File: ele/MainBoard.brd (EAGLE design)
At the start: 149.3 x 100 mm, 114 parts, among them IC1 MCP23017SP, IC2 74HC595D, IC3 74HC595D, X1 POWER_IN, X2 POWER_OUT

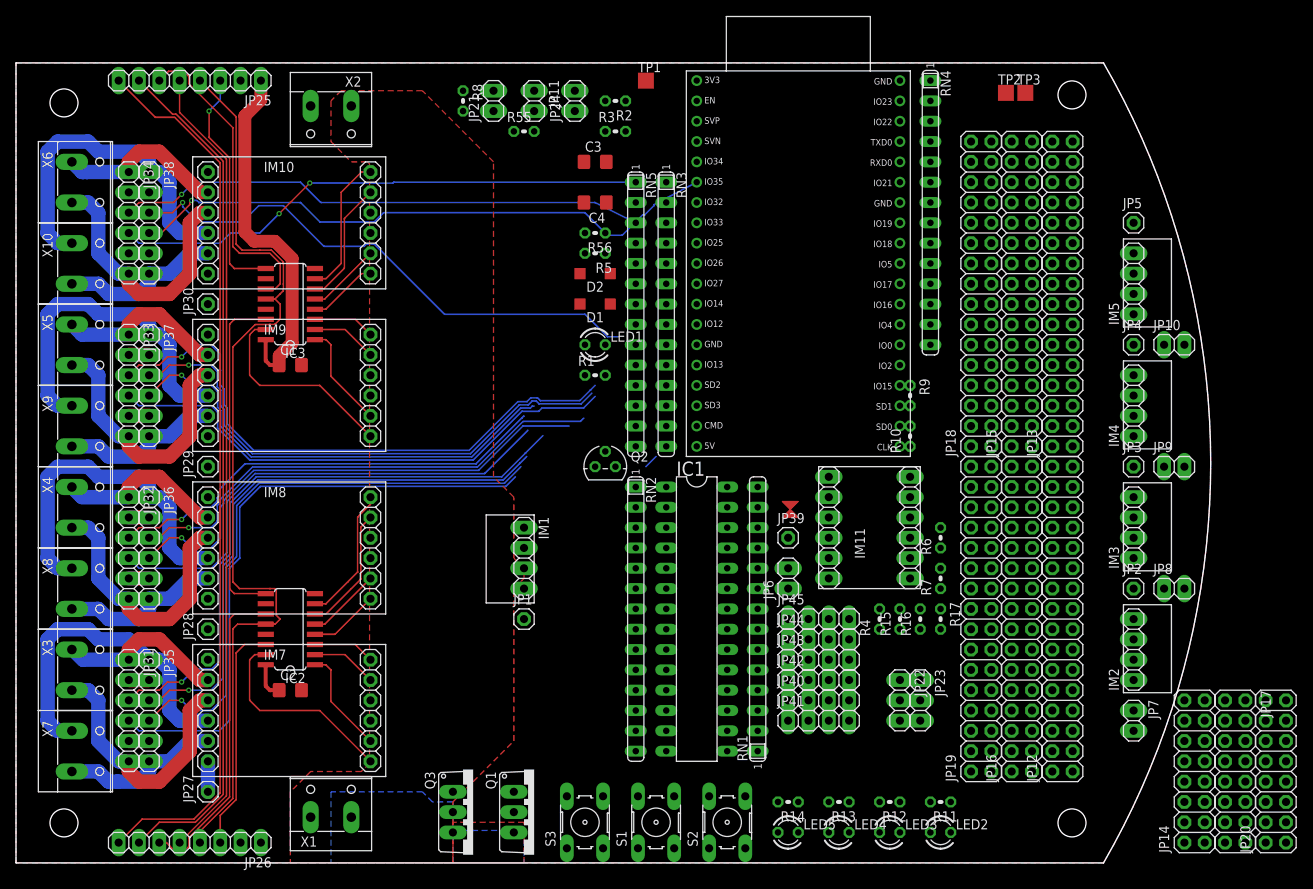
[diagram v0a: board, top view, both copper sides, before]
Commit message: ele: Route signals
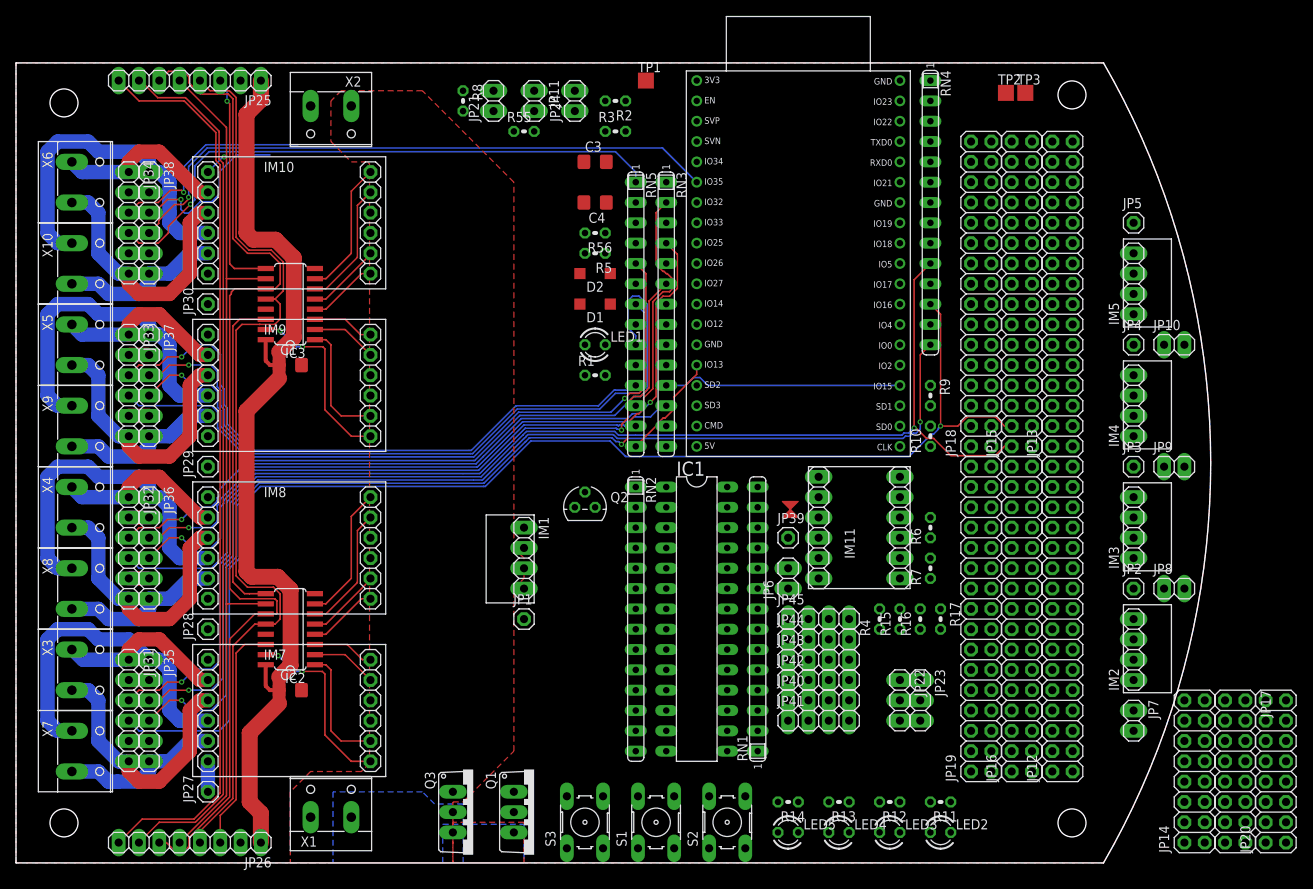
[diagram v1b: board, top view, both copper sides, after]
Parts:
- moved Q2 5.68 mm to (71.1, 44.5)
- moved R10 2.54 mm to (114.3, 53.3)
- moved R9 2.54 mm to (114.3, 58.4)
- moved R6 1.80 mm to (114.3, 41.9)
- moved R7 1.80 mm to (114.3, 36.8)
- moved IM11 1.27 mm to (111.8, 34.3)
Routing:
- net ENC1A: track 76.3 -> 160.4 mm, vias 1 -> 2
- net ENC1B: track 76.9 -> 160.0 mm, vias 0 -> 1
- net +3V3: track 50.1 -> 118.5 mm
- net ENC2A: track 71.8 -> 133.9 mm, vias 1 -> 2
- net SCKMOT: track 79.2 -> 130.3 mm
- net ENC2B: track 75.6 -> 123.4 mm, vias 1 -> 2
- net ENC8A: track 68.4 -> 21.9 mm
- net ENC7A: track 66.6 -> 26.8 mm
- net ENC3A: track 56.4 -> 95.3 mm, vias 1 -> 2
- net ENC3B: track 61.3 -> 94.3 mm, vias 0 -> 1
- net ENC6B: track 58.4 -> 89.2 mm, vias 1 -> 2
- net ENC4A_: track 0.00 -> 30.0 mm
- net ENC5B: track 66.1 -> 92.6 mm
- net ENC6A: track 67.3 -> 84.7 mm
- net ENC4B_: track 0.00 -> 13.5 mm
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
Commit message: ele: Route more signals
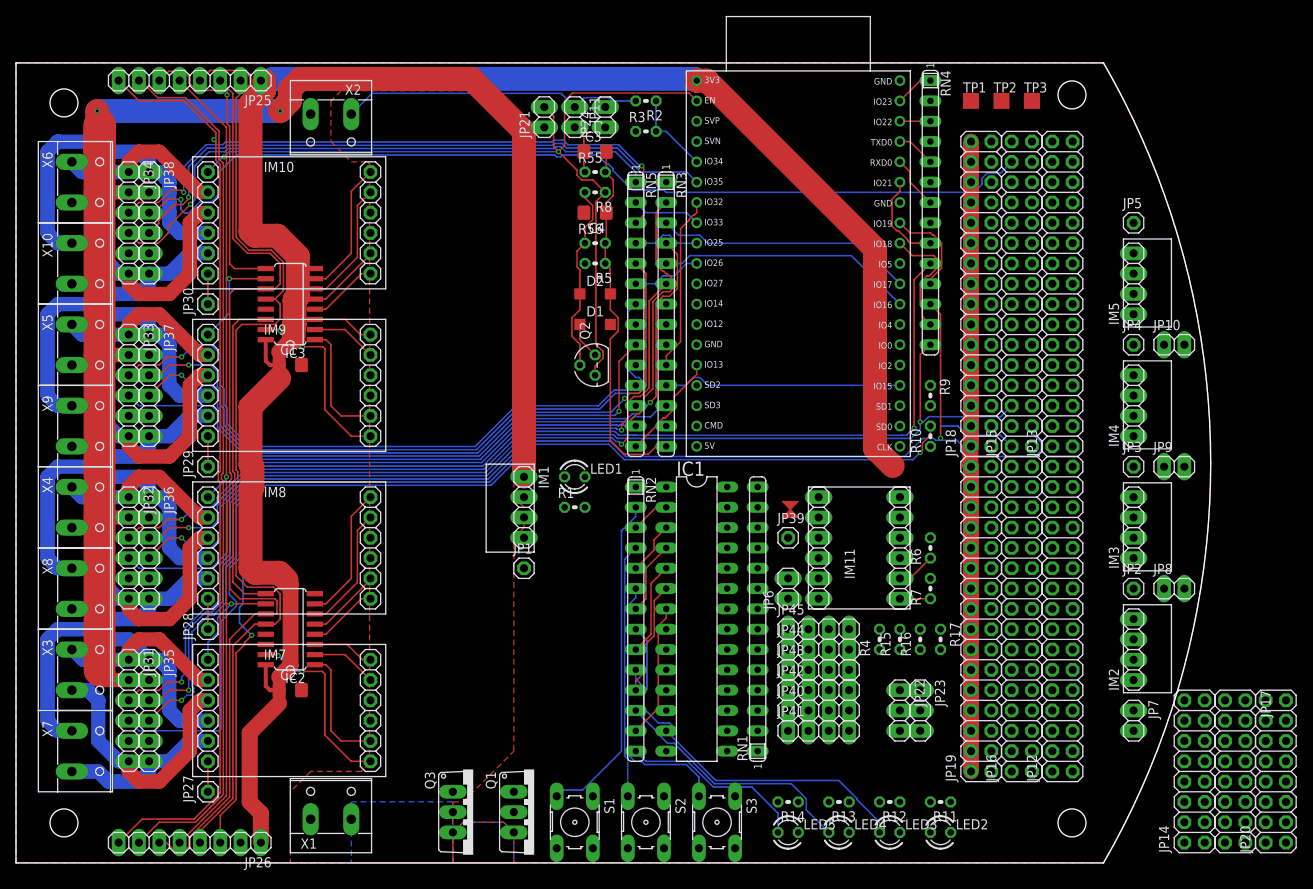
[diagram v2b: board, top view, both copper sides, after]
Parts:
- moved TP1 40.7 mm to (119.4, 95.2)
- moved R8 20.1 mm to (72.4, 83.8), turned to 180 degrees
- moved Q2 17.8 mm to (72.4, 62.2), turned to 90 degrees
- moved LED1 16.7 mm to (69.8, 48.3)
- moved R1 16.7 mm to (69.8, 44.5)
- moved S3 16.5 mm to (87.6, 5.08), turned to 270 degrees
- moved R55 10.2 mm to (72.4, 86.4)
- moved S1 10.2 mm to (69.8, 5.08), turned to 270 degrees
- moved S2 10.2 mm to (78.7, 5.08), turned to 270 degrees
- moved JP21 6.67 mm to (66.0, 93.2)
- moved IM1 6.35 mm to (64.8, 49.5)
- moved JP1 6.35 mm to (63.5, 36.8)
- moved JP11 5.47 mm to (69.8, 93.2)
- moved JP24 4.32 mm to (73.7, 93.2)
- moved R2 3.81 mm to (78.7, 95.2)
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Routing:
- net +3V3: track 118.5 -> 335.2 mm
- net +5V: track 7.62 -> 203.1 mm, vias 0 -> 2
- net EN: track 113.1 -> 237.7 mm, vias 1 -> 5
- net SERMOT: track 28.7 -> 140.2 mm, vias 0 -> 2
- net ENC8A: track 21.9 -> 118.9 mm
- net ENC7A: track 26.8 -> 78.9 mm, vias 1 -> 2
- net ESP_!SHUTDOWN: track 0.00 -> 46.8 mm
- net EB4: track 0.00 -> 43.0 mm
- net EB0: track 0.00 -> 41.6 mm
- net VCC: track 0.00 -> 38.0 mm
- net EB2: track 0.00 -> 33.6 mm
- net ENC3A_: track 0.00 -> 32.4 mm
- net ENC3B_: track 0.00 -> 32.1 mm
- net EB1: track 0.00 -> 31.8 mm
- net EB5: track 0.00 -> 31.3 mm
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
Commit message: ele: Route even more signals
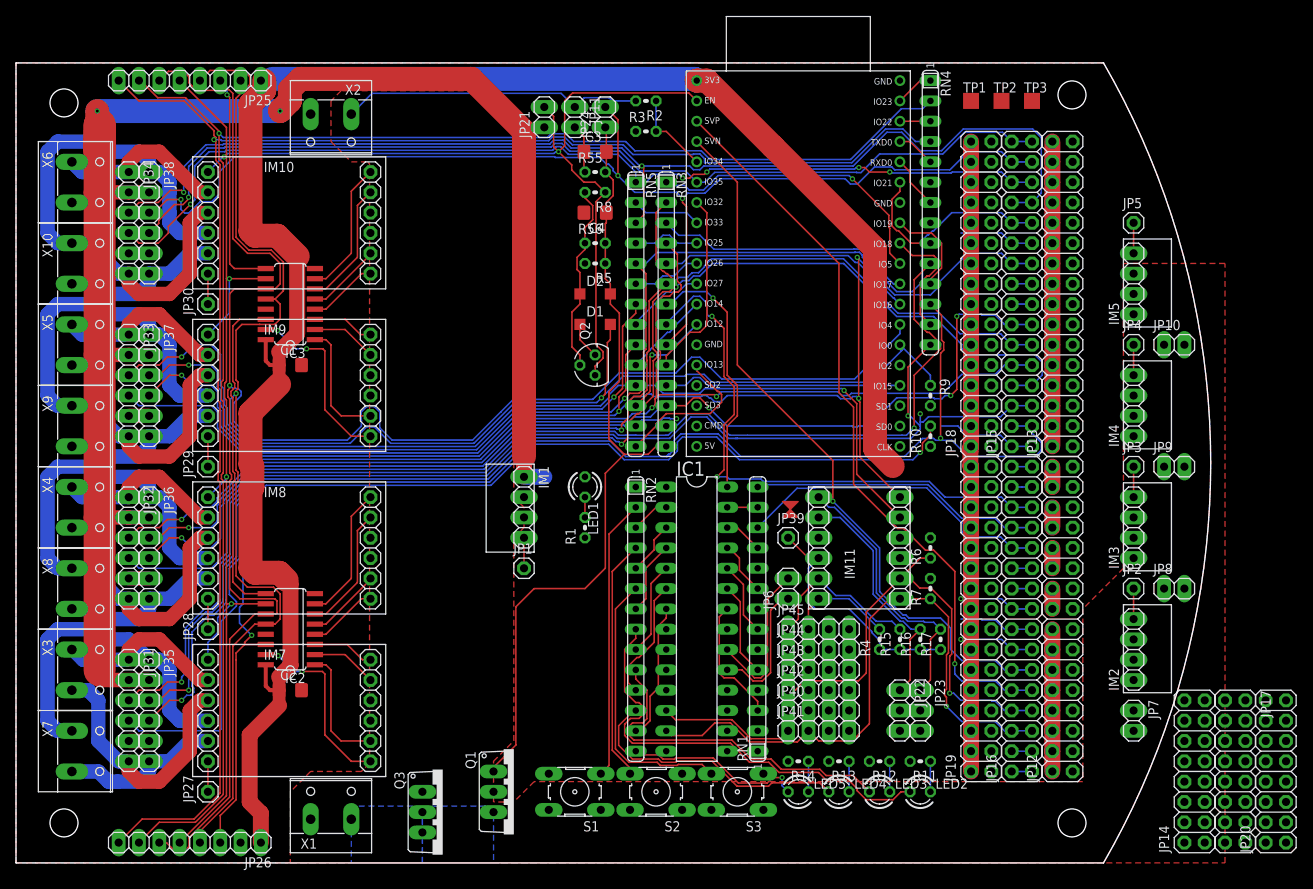
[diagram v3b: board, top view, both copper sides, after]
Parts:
- moved LED2 5.68 mm to (113.0, 8.89)
- moved R11 5.68 mm to (113.0, 12.7)
- moved LED5 5.24 mm to (97.8, 8.89)
- moved R14 5.24 mm to (97.8, 12.7)
- moved LED3 5.24 mm to (108.0, 8.89)
- moved R12 5.24 mm to (108.0, 12.7)
- moved LED4 5.08 mm to (102.9, 8.89)
- moved R13 5.08 mm to (102.9, 12.7)
- moved S3 4.58 mm to (90.2, 8.89), turned to 180 degrees
- moved S2 4.02 mm to (80.0, 8.89), turned to 180 degrees
- moved S1 3.81 mm to (69.8, 8.89), turned to 180 degrees
- moved Q3 3.81 mm to (53.3, 6.35)
- moved Q1 3.59 mm to (62.2, 8.89)
- moved R1 2.84 mm to (71.1, 41.9), turned to 90 degrees
- moved LED1 1.80 mm to (71.1, 47.0), turned to 270 degrees
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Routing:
- net SDA: track 112.8 -> 285.6 mm, vias 0 -> 2
- net SCL: track 118.3 -> 288.6 mm, vias 1 -> 2
- net RCKMOT: track 124.2 -> 238.2 mm, vias 0 -> 2
- net SCKMOT: track 130.9 -> 235.9 mm, vias 0 -> 1
- net IO36: track 0.00 -> 94.0 mm, vias 0 -> 1
- net ENC5B: track 77.1 -> 168.0 mm, vias 1 -> 3
- net IO39: track 0.00 -> 90.4 mm, vias 0 -> 1
- net EA7: track 0.00 -> 72.1 mm, vias 0 -> 2
- net ENC7A: track 78.9 -> 144.6 mm
- net ENC6B: track 88.8 -> 148.8 mm
- net ENC4A: track 72.9 -> 132.4 mm, vias 1 -> 4
- net ENC2B: track 120.3 -> 179.5 mm, vias 2 -> 3
- net ESP_!SHUTDOWN: track 46.8 -> 100.3 mm
- net ENC7B: track 74.5 -> 126.0 mm, vias 1 -> 5
- net ENC3B: track 94.3 -> 145.8 mm
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- removed copper zone on layer 1, net BATT_CATHODE2

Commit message: ele: Remove impossible headers, route signals
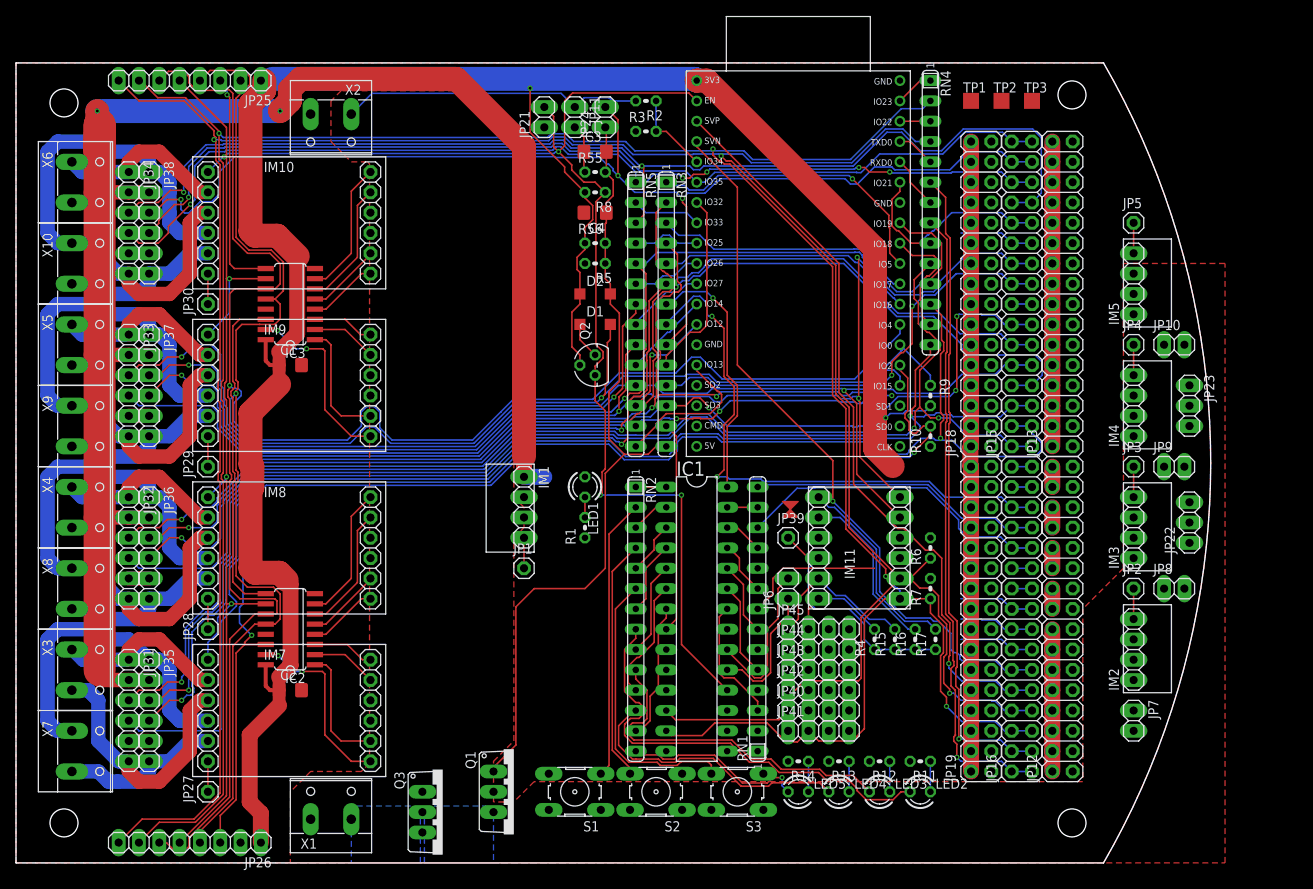
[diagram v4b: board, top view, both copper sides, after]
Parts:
- removed JP14: 5V_GND_3, pinhead:2X08
- removed JP17: SIG3, pinhead:2X08
- removed JP20: 3V3_GND_3, pinhead:2X08
- moved JP23 50.8 mm to (146.7, 57.1)
- moved JP22 43.2 mm to (146.7, 42.5), turned to 90 degrees
- moved R16 0.64 mm to (112.4, 27.9)
- moved R4 0.64 mm to (107.3, 27.9)
- moved R15 0.63 mm to (109.9, 27.9)
- moved R17 0.63 mm to (114.9, 27.9)
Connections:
- net +3V3: no longer JP20.10, JP20.12, JP20.14, JP20.16, JP20.2, JP20.4, JP20.6, JP20.8
- net 5V_2: no longer JP14.10, JP14.12, JP14.14, JP14.16, JP14.2, JP14.4, JP14.6, JP14.8
- net EB0: no longer JP17.1, JP17.2
- net EB1: no longer JP17.3, JP17.4
- net EB2: no longer JP17.5, JP17.6
- net EB3: no longer JP17.7, JP17.8
- net EB4: no longer JP17.10, JP17.9
- net EB5: no longer JP17.11, JP17.12
- net EB6: no longer JP17.13, JP17.14
- net ESP_!SHUTDOWN: no longer JP17.15, JP17.16
- net GND: no longer JP14.1, JP14.11, JP14.13, JP14.15, JP14.3, JP14.5, JP14.7, JP14.9, JP20.1, JP20.11, JP20.13, JP20.15, JP20.3, JP20.5, JP20.7, JP20.9
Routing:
- net TXD0: track 2.54 -> 81.2 mm, vias 0 -> 1
- net RXD0: track 2.54 -> 79.1 mm, vias 0 -> 1
- net SDA: track 285.6 -> 352.7 mm, vias 2 -> 4
- net SCL: track 288.6 -> 349.0 mm, vias 2 -> 3
- net EN: track 238.3 -> 291.0 mm, vias 5 -> 7
- net ENC5A: track 126.3 -> 158.0 mm, vias 2 -> 4
- net +3V3: track 335.2 -> 365.1 mm, vias 0 -> 2
- net ENC4B: track 79.5 -> 107.9 mm, vias 2 -> 4
- net ESP_!SHUTDOWN!_: track 0.00 -> 26.5 mm
- net EA3: track 2.54 -> 20.4 mm
- net SERMOT: track 143.2 -> 154.6 mm
- net A5V: track 30.4 -> 21.0 mm
- net B5V: track 33.9 -> 24.6 mm
- net +5V: track 223.4 -> 227.4 mm
- net EB0_: track 0.00 -> 3.81 mm
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
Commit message: ele: Return impossible headers, shrink board, route signals
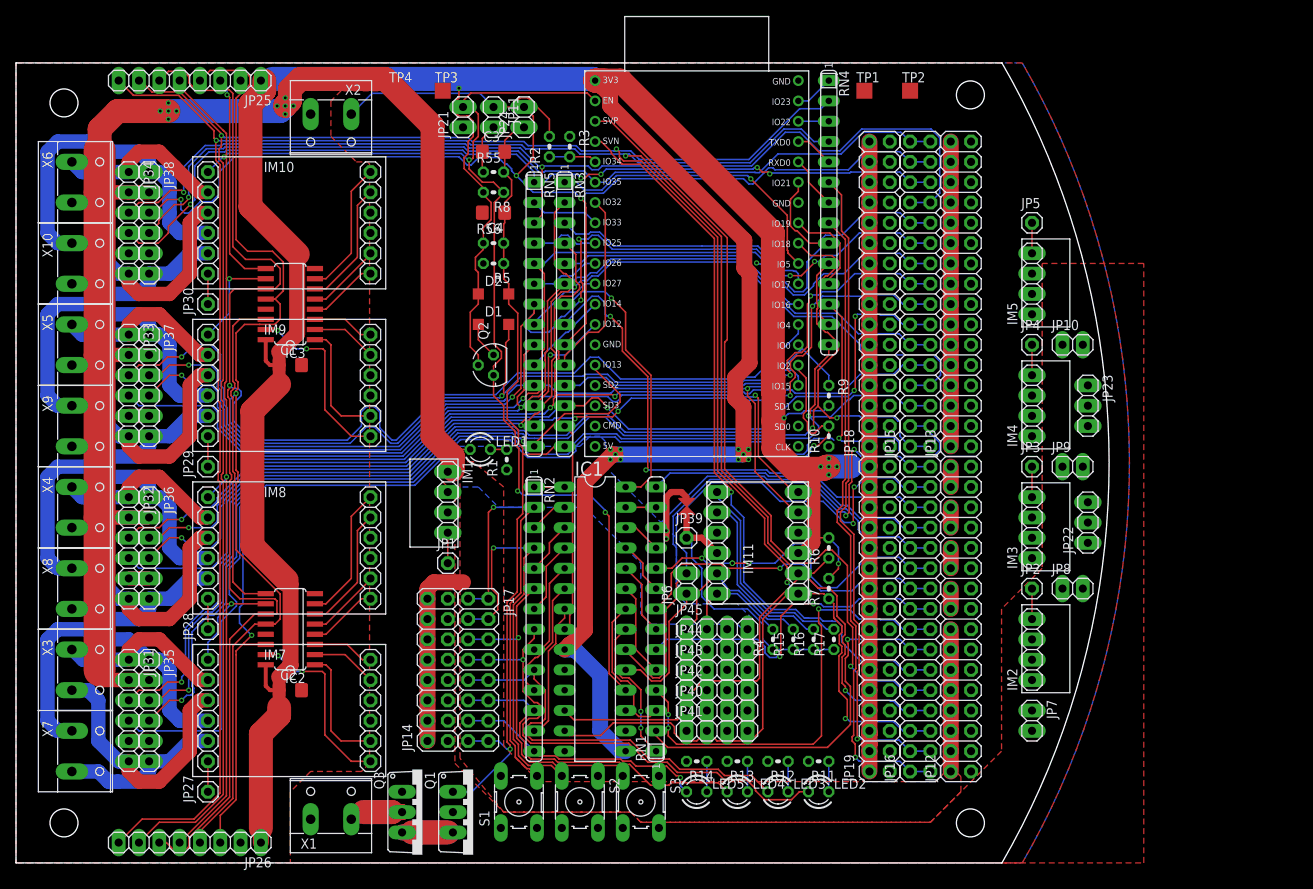
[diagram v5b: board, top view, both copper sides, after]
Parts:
- added JP14: 5V_GND_3, pinhead:2X08
- added JP17: SIG3, pinhead:2X08
- added TP4: TPTP20SQ, testpad:TP20SQ
- moved TP3 73.7 mm to (53.3, 96.5)
- moved LED1 13.9 mm to (58.0, 51.7), turned to 0 degrees
- moved TP1 13.4 mm to (106.0, 96.5)
- moved R2 13.4 mm to (66.7, 89.5), turned to 90 degrees
- moved R1 13.0 mm to (61.3, 50.4)
- moved U$2 13.0 mm to (84.8, 43.6)
- moved IM11 12.7 mm to (99.1, 32.4)
- moved JP6 12.7 mm to (83.8, 34.9)
- moved C3 12.7 mm to (59.7, 88.9)
- moved C4 12.7 mm to (59.7, 81.3)
- moved D1 12.7 mm to (59.7, 67.3)
- moved D2 12.7 mm to (59.7, 71.1)
- moved IC1 12.7 mm to (72.4, 30.5)
- moved IM2 12.7 mm to (125.7, 21.6)
- moved IM3 12.7 mm to (125.7, 36.8)
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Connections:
- net +5V: now also JP14.10, JP14.12, JP14.14, JP14.16, JP14.2, JP14.4, JP14.6, JP14.8, TP4.TP
- net EB0: now also JP17.1, JP17.2
- net EB1: now also JP17.3, JP17.4
- net EB2: now also JP17.5, JP17.6
- net EB3: now also JP17.7, JP17.8
- net EB4: now also JP17.10, JP17.9
- net EB5: now also JP17.11, JP17.12
- net EB6: now also JP17.13, JP17.14
- net ESP_!SHUTDOWN: now also JP17.15, JP17.16
- net GND: now also JP14.1, JP14.11, JP14.13, JP14.15, JP14.3, JP14.5, JP14.7, JP14.9
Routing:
- net +3V3: track 365.1 -> 513.2 mm, vias 2 -> 18
- net EINT1: track 19.1 -> 72.3 mm, vias 0 -> 2
- net EA1: track 9.42 -> 57.4 mm, vias 0 -> 3
- net ENC6A: track 91.3 -> 138.5 mm, vias 2 -> 6
- net EINT0: track 22.1 -> 68.9 mm, vias 0 -> 2
- net EA4: track 2.54 -> 42.4 mm, vias 0 -> 4
- net EA0: track 9.42 -> 48.7 mm, vias 0 -> 1
- net EA2: track 9.42 -> 43.1 mm, vias 0 -> 2
- net ENC5B: track 167.9 -> 137.0 mm
- net +5V: track 227.4 -> 251.3 mm, vias 2 -> 12
- net EA3: track 20.4 -> 41.7 mm, vias 0 -> 1
- net EB1: track 30.4 -> 51.2 mm, vias 0 -> 1
- net EB0: track 35.1 -> 55.7 mm, vias 0 -> 1
- net EA0_: track 0.00 -> 18.6 mm, vias 0 -> 2
- net EN: track 291.0 -> 272.8 mm
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- added copper zone on layer 1, net +5V
- added copper zone on layer 16, net +5V
- removed copper zone on layer 16, net BATT_CATHODE
- removed copper zone on layer 16, net BATT_CATHODE2
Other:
- board size 149.3 x 100 mm -> 136.6 x 100 mm

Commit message: ele: Route more wires still!
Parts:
- moved JP23 14.0 mm to (134.0, 43.2)
- moved JP22 13.3 mm to (134.0, 55.9)
- moved R1 11.1 mm to (60.3, 39.4)
- moved LED1 7.59 mm to (60.3, 44.5), turned to 270 degrees
- moved U$2 0.90 mm to (84.2, 42.9)
- moved JP10 0.64 mm to (131.4, 64.8)
- moved JP8 0.64 mm to (131.4, 34.3)
- moved JP9 0.64 mm to (131.4, 49.5)
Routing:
- net B5V: track 26.6 -> 172.7 mm, vias 0 -> 2
- net A5V: track 22.7 -> 165.7 mm, vias 0 -> 1
- net 5V_4: track 2.54 -> 29.8 mm
- net +3V3: track 513.2 -> 536.9 mm
- net 5V_2: track 40.6 -> 58.4 mm
- net ENC5B: track 137.0 -> 153.6 mm
- net 5V_5: track 2.54 -> 18.3 mm
- net EB0: track 55.7 -> 42.8 mm
- net +5V: track 251.3 -> 239.0 mm
- net SDA: track 341.8 -> 348.0 mm
- net SCL: track 337.5 -> 343.2 mm
- net 5V_3: track 2.54 -> 7.67 mm
- net IO39: track 94.1 -> 99.2 mm
- net IO36: track 99.3 -> 104.4 mm
- net N$9: track 2.03 -> 0.00 mm
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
